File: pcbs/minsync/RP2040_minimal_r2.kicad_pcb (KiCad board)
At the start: 2 copper layers, 42 x 42 mm, 46 parts, among them J1 SWD_JST, J3 POWER, J5 SWD_HEADERS, J6 Conn_01x01_Pin, J7 SSD1306, SW1 SW_Push, U1 NCP1117-3.3_SOT223, U2 W25Q128JVS, U3 RP2040, U4 Si5351A-B-GT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

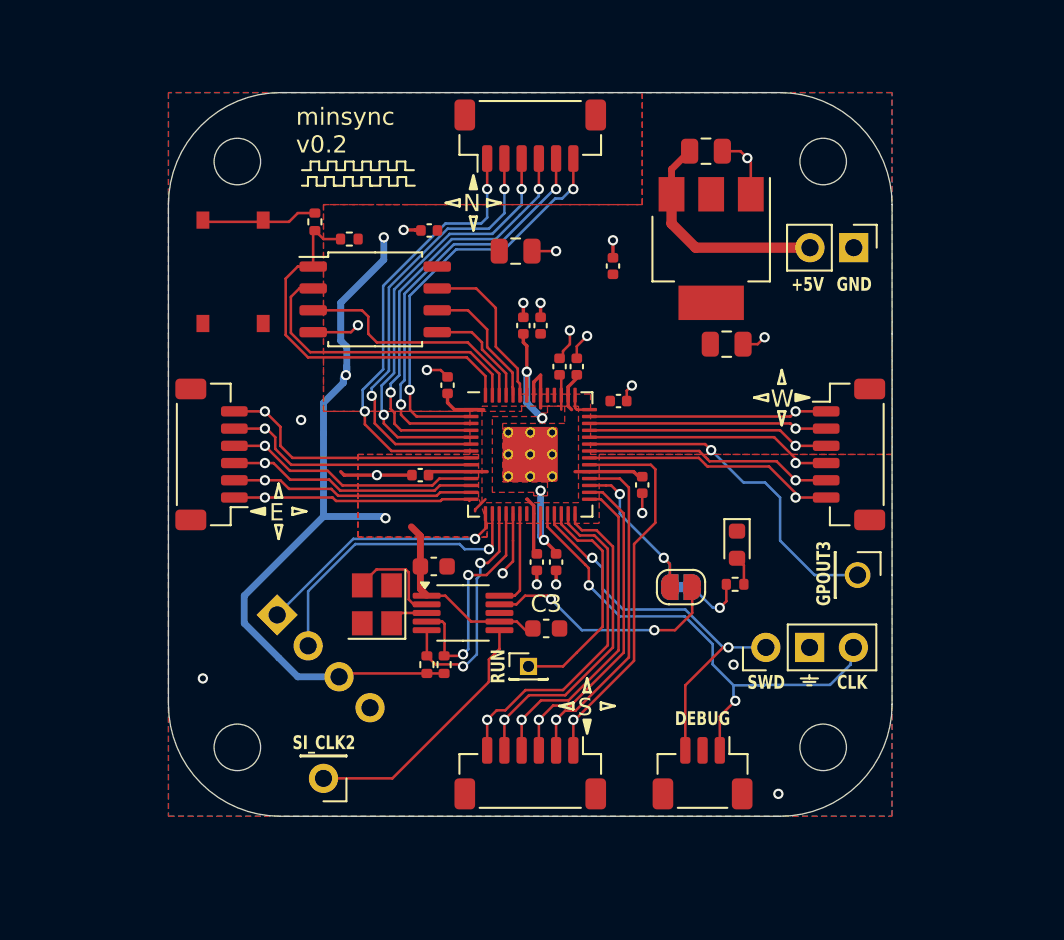
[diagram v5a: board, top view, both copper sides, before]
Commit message: Fix button, reroute some tracks
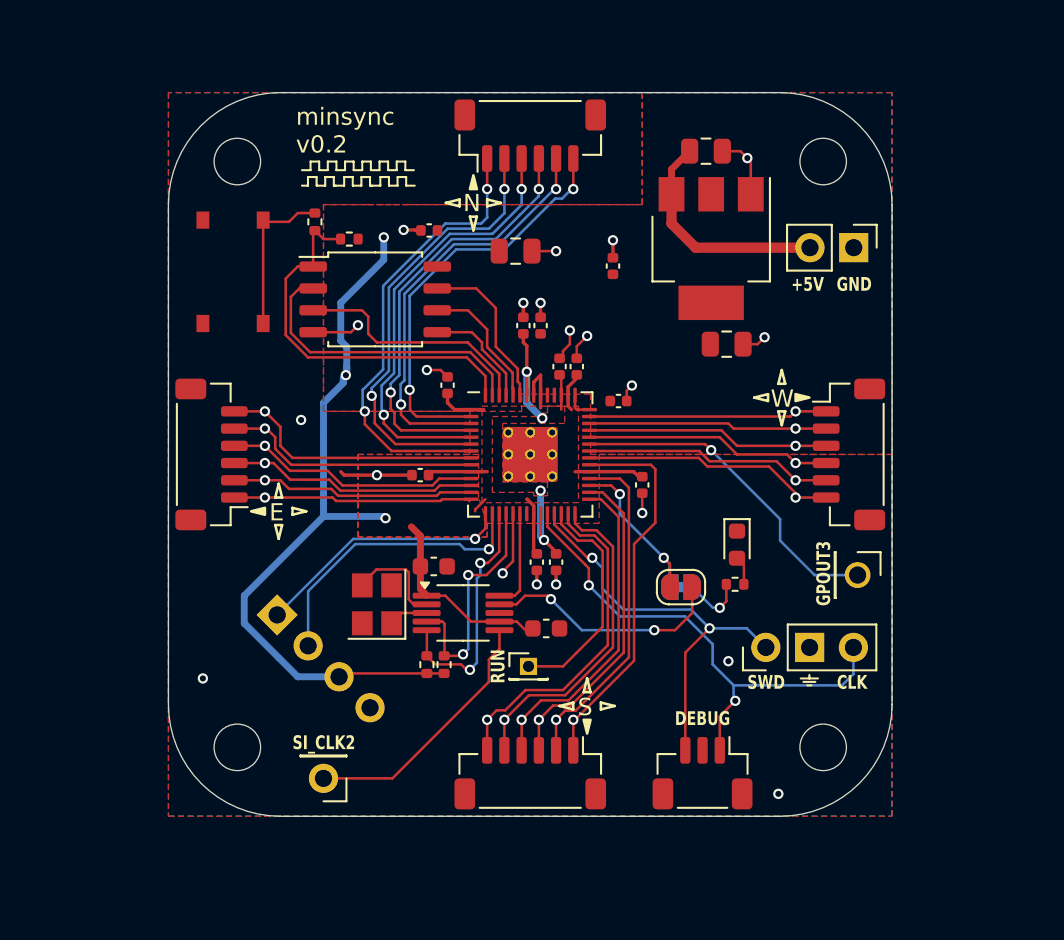
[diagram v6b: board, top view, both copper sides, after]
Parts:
- R4, R5: value 4.7k -> 2.2k
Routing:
- net /~{USB_BOOT}: track 6.71 -> 9.21 mm
- net /GPIO25: track 20.2 -> 19.4 mm
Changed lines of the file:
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@@
 			)
 		)
-		(property "Value" "4.7k"
+		(property "Value" "2.2k"
 			(at 0 1.17 90)
 			(layer "F.Fab")
@@
 			)
 		)
-		(property "Value" "4.7k"
+		(property "Value" "2.2k"
 			(at 0 1.17 90)
 			(layer "F.Fab")
@@
 			(at 0 -1.43 0)
 			(layer "F.SilkS")
+			(hide yes)
 			(effects
 				(font
@@
 		)
 		(pad "1" smd rect
-			(at -3 1.5 90)
+			(at 3 -2 90)
 			(size 1 0.75)
 			(layers "F.Cu" "F.Paste" "F.Mask")
@@
 		)
 		(pad "2" smd rect
-			(at 3 -2 90)
+			(at -3 1.5 90)
 			(size 1 0.75)
 			(layers "F.Cu" "F.Paste" "F.Mask")
@@
 	)
 	(via
-		(at 111.8 112.2)
-		(size 0.6)
-		(drill 0.35)
-		(layers "F.Cu" "B.Cu")
-		(free yes)
-		(net 1)
-	)
-	(via
 		(at 81 113)
 		(size 0.6)
@@
 	)
 	(via
+		(at 111.5 112)
+		(size 0.6)
+		(drill 0.35)
+		(layers "F.Cu" "B.Cu")
+		(free yes)
+		(net 1)
+	)
+	(via
 		(at 100.6 91.205)
 		(size 0.6)
@@
 	)
 	(segment
-		(start 84.5 86.5)
-		(end 81 86.5)
+		(start 86.51 85.99)
+		(end 86 86.5)
 		(width 0.15)
 		(layer "F.Cu")
@@
 	)
 	(segment
-		(start 86.51 85.99)
-		(end 86 86.5)
+		(start 84.5 86.4)
+		(end 84.5 92.4)
 		(width 0.15)
 		(layer "F.Cu")
@@
 	(segment
 		(start 95.985 112.185)
-		(end 96.1 112.3)
+		(end 96.3 112.5)
 		(width 0.15)
 		(layer "F.Cu")
@@
 	)
 	(segment
+		(start 96.3 112.5)
+		(end 96.5 112.5)
+		(width 0.15)
+		(layer "F.Cu")
+		(net 9)
+	)
+	(segment
 		(start 94 110.2125)
 		(end 93.9875 110.2)
@@
 	)
 	(via
-		(at 96.1 112.3)
+		(at 96.5 112.5)
 		(size 0.6)
 		(drill 0.35)
@@
 	)
 	(segment
-		(start 97.1 107)
-		(end 97.1 106.3)
-		(width 0.15)
-		(layer "B.Cu")
-		(net 9)
-	)
-	(segment
-		(start 96.2 112.3)
-		(end 96.1 112.3)
+		(start 96.9 112.1)
+		(end 96.5 112.5)
 		(width 0.15)
 		(layer "B.Cu")
@@
 	)
 	(segment
-		(start 96.9 111.6)
+		(start 97.1 107)
 		(end 96.9 107.2)
 		(width 0.15)
@@
 	)
 	(segment
-		(start 96.9 111.6)
-		(end 96.2 112.3)
+		(start 96.9 107.2)
+		(end 96.9 112.1)
 		(width 0.15)
 		(layer "B.Cu")
@@
 	)
 	(segment
-		(start 96.9 107.2)
+		(start 97.1 106.3)
 		(end 97.1 107)
 		(width 0.15)
@@
 	)
 	(segment
-		(start 115.1 98.2)
-		(end 115.4 98.5)
+		(start 103.4375 98.2)
+		(end 111.5 98.2)
 		(width 0.15)
 		(layer "F.Cu")
@@
 	)
 	(segment
-		(start 117.175 98.5)
-		(end 115.4 98.5)
+		(start 115.4 98.5)
+		(end 111.8 98.5)
 		(width 0.15)
 		(layer "F.Cu")
@@
 	)
 	(segment
-		(start 103.4375 98.2)
-		(end 115.1 98.2)
+		(start 111.8 98.5)
+		(end 111.5 98.2)
+		(width 0.15)
+		(layer "F.Cu")
+		(net 25)
+	)
+	(segment
+		(start 117.175 98.5)
+		(end 115.4 98.5)
 		(width 0.15)
 		(layer "F.Cu")
@@
 	)
 	(segment
-		(start 103.4375 98.6)
-		(end 114.5 98.6)
+		(start 111.1 98.6)
+		(end 112 99.5)
 		(width 0.15)
 		(layer "F.Cu")
@@
 	)
 	(segment
-		(start 114.5 98.6)
+		(start 112 99.5)
 		(end 115.4 99.5)
 		(width 0.15)
@@
 	)
 	(segment
+		(start 103.4375 98.6)
+		(end 111.1 98.6)
+		(width 0.15)
+		(layer "F.Cu")
+		(net 26)
+	)
+	(segment
 		(start 117.175 99.5)
 		(end 115.4 99.5)
@@
 	)
 	(segment
-		(start 115.4 100.242463)
+		(start 114.9 100)
 		(end 115.4 100.5)
 		(width 0.15)
@@
 	)
 	(segment
-		(start 114.157537 99)
-		(end 115.4 100.242463)
+		(start 111 99)
+		(end 112 100)
+		(width 0.15)
+		(layer "F.Cu")
+		(net 27)
+	)
+	(segment
+		(start 112 100)
+		(end 114.9 100)
 		(width 0.15)
 		(layer "F.Cu")
@@
 	(segment
 		(start 103.4375 99)
-		(end 114.157537 99)
+		(end 111 99)
 		(width 0.15)
 		(layer "F.Cu")
@@
 	)
 	(segment
-		(start 110.5 99.75)
-		(end 112.375 101.625)
+		(start 114.5 105)
+		(end 116.5 107)
 		(width 0.15)
 		(layer "B.Cu")
@@
 	)
 	(segment
-		(start 114.5 105)
-		(end 116.5 107)
-		(width 0.15)
-		(layer "B.Cu")
-		(net 28)
-	)
-	(segment
-		(start 114.5 102.5)
+		(start 114.5 103.75)
 		(end 114.5 105)
 		(width 0.15)
@@
 	)
 	(segment
-		(start 113.625 101.625)
-		(end 114.5 102.5)
-		(width 0.15)
-		(layer "B.Cu")
-		(net 28)
-	)
-	(segment
-		(start 112.375 101.625)
-		(end 113.625 101.625)
+		(start 110.5 99.75)
+		(end 114.5 103.75)
 		(width 0.15)
 		(layer "B.Cu")
@@
 	)
 	(segment
-		(start 109 113.4)
-		(end 109 117.175)
+		(start 109 111.5)
+		(end 110.408732 110.091268)
 		(width 0.15)
 		(layer "F.Cu")
@@
 	)
 	(segment
-		(start 111.5 111.2)
-		(end 111.2 111.2)
-		(width 0.15)
-		(layer "F.Cu")
-		(net 39)
-	)
-	(segment
 		(start 103.327208 106)
 		(end 103.6 106)
@@
 	)
 	(segment
-		(start 111.2 111.2)
-		(end 109 113.4)
+		(start 109 117.175)
+		(end 109 111.5)
 		(width 0.15)
 		(layer "F.Cu")
@@
 	)
 	(via
-		(at 111.5 111.2)
+		(at 110.408732 110.091268)
 		(size 0.6)
 		(drill 0.35)
@@
 	)
 	(segment
-		(start 105.4 109)
-		(end 104.2 107.8)
+		(start 109.317464 109)
+		(end 105.4 109)
 		(width 0.15)
 		(layer "B.Cu")
@@
 	)
 	(segment
-		(start 111.5 111.2)
-		(end 113.675 111.2)
+		(start 104.2 106.6)
+		(end 103.6 106)
 		(width 0.15)
 		(layer "B.Cu")
@@
 	)
 	(segment
-		(start 104.2 106.6)
-		(end 103.6 106)
+		(start 113.675 111.2)
+		(end 112.566268 110.091268)
 		(width 0.15)
 		(layer "B.Cu")
@@
 	)
 	(segment
-		(start 109 109)
-		(end 105.4 109)
+		(start 105.4 109)
+		(end 104.2 107.8)
 		(width 0.15)
 		(layer "B.Cu")
@@
 	)
 	(segment
-		(start 109 109)
-		(end 111.2 111.2)
+		(start 104.2 107.8)
+		(end 104.2 106.6)
 		(width 0.15)
 		(layer "B.Cu")
@@
 	)
 	(segment
-		(start 104.2 107.8)
-		(end 104.2 106.6)
+		(start 112.566268 110.091268)
+		(end 110.408732 110.091268)
 		(width 0.15)
 		(layer "B.Cu")
@@
 	)
 	(segment
-		(start 111.2 111.2)
-		(end 111.5 111.2)
+		(start 110.408732 110.091268)
+		(end 109.317464 109)
 		(width 0.15)
 		(layer "B.Cu")
@@
 	)
 	(segment
-		(start 113.575 113.4)
-		(end 113.6 113.375)
-		(width 0.15)
-		(layer "B.Cu")
-		(net 40)
-	)
-	(segment
 		(start 110.5875 111.0125)
 		(end 110.5875 112.1875)
@@
 	)
 	(segment
-		(start 111.8 113.4)
-		(end 113.3 113.4)
+		(start 118.1 113.4)
+		(end 118.754999 112.745001)
 		(width 0.15)
 		(layer "B.Cu")
@@
 	)
 	(segment
-		(start 118.6 111.354999)
+		(start 118.754999 112.745001)
 		(end 118.754999 111.2)
 		(width 0.15)
@@
 	)
 	(segment
-		(start 113.3 113.4)
-		(end 113.575 113.4)
+		(start 111.8 113.4)
+		(end 118.1 113.4)
 		(width 0.15)
 		(layer "B.Cu")
@@
 		(width 0.15)
 		(layer "B.Cu")
-		(net 40)
-	)
-	(segment
-		(start 118.6 112.2)
-		(end 118.6 111.354999)
-		(width 0.15)
-		(layer "B.Cu")
-		(net 40)
-	)
-	(segment
-		(start 117.4 113.375)
-		(end 118.575 112.2)
-		(width 0.15)
-		(layer "B.Cu")
-		(net 40)
-	)
-	(segment
-		(start 118.575 112.2)
-		(end 118.6 112.2)
-		(width 0.15)
-		(layer "B.Cu")
-		(net 40)
-	)
-	(segment
-		(start 113.6 113.375)
-		(end 117.4 113.375)
-		(width 0.15)
-		(layer "B.Cu")
